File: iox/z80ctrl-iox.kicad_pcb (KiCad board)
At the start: 2 copper layers, 99.8 x 49.9 mm, 29 parts, among them J1 BUS, J10 GPIO_A, J11 RESET, J2 BUSEXT, J3 SPI1, J4 SPI2, J5 SPI3, J6 SPI4, J7 GPIO_B, J8 GPIO_C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

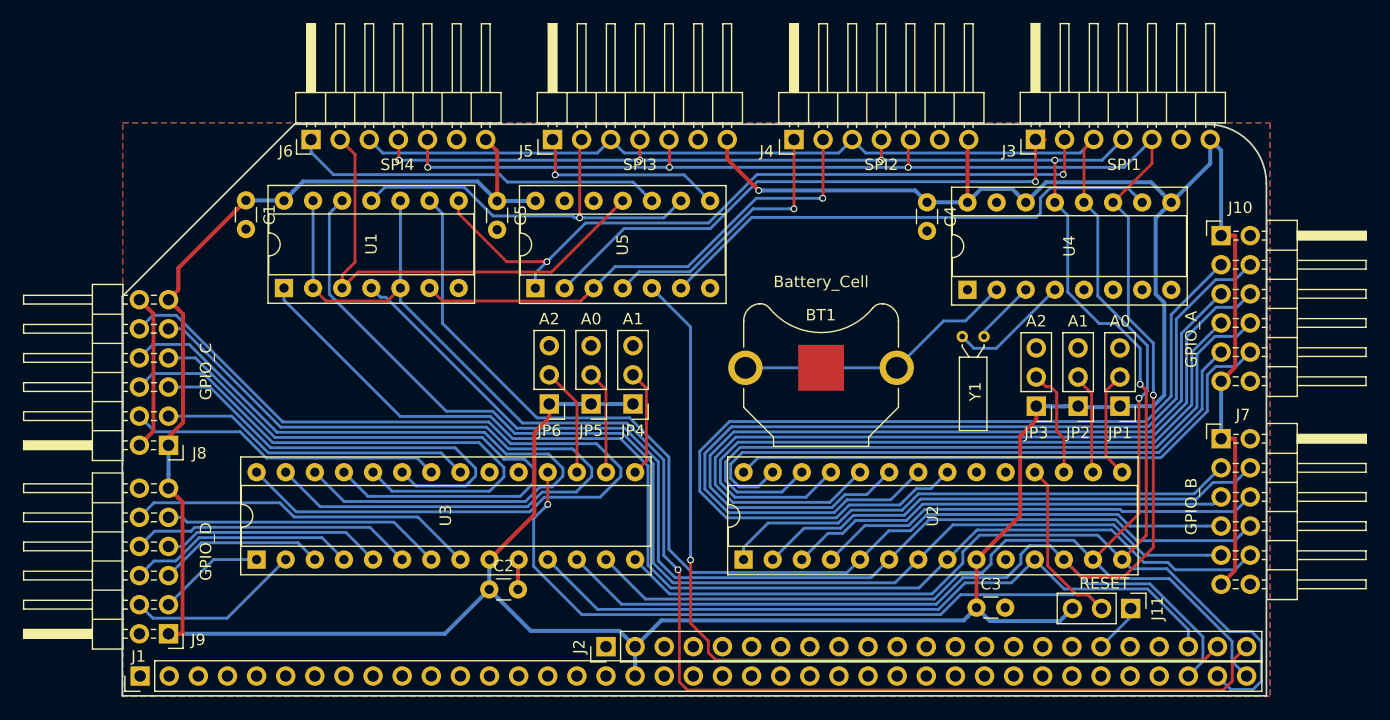
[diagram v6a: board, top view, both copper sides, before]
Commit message: Upgrade Kicad projects to v6
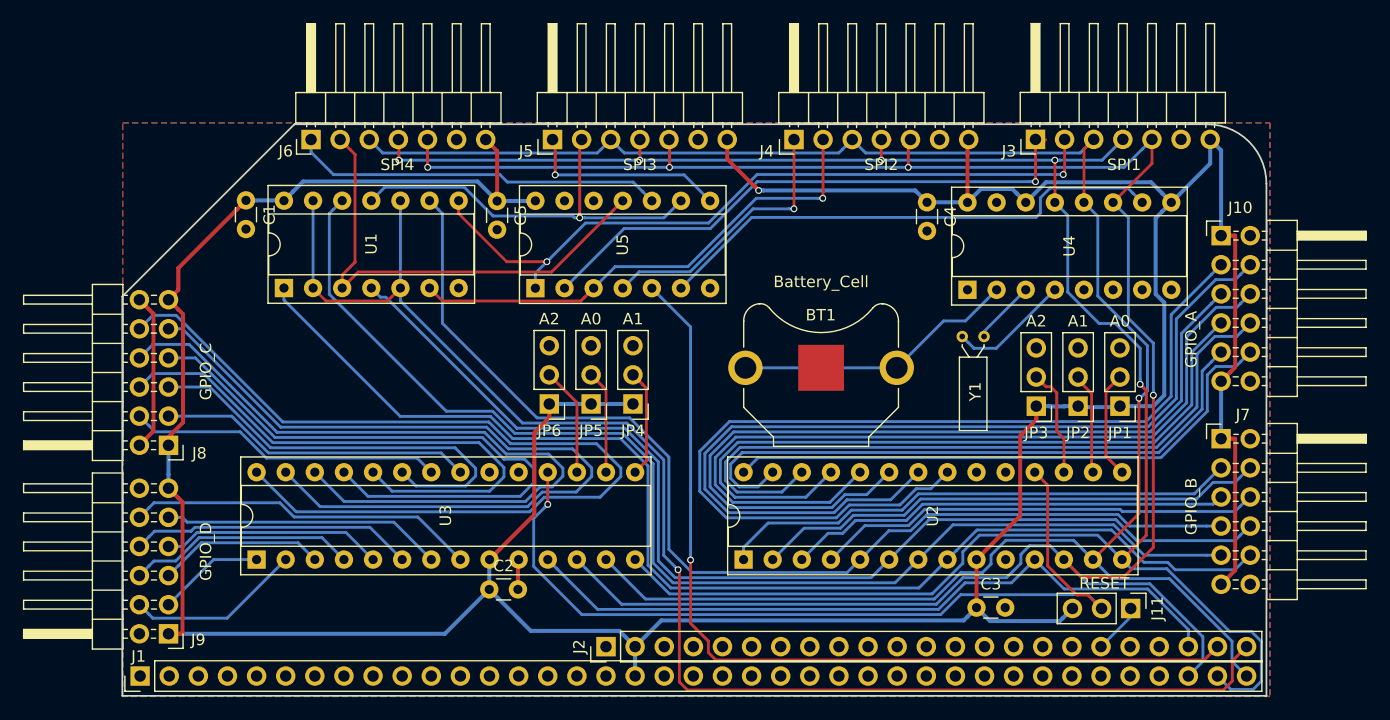
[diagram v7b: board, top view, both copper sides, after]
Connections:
- net /~AUXCS1~ renamed /~{AUXCS1}
- net /~AUXCS2~ renamed /~{AUXCS2}
- net /~AVRRST~ renamed /~{AVRRST}
- net /~EXTCS1~ renamed /~{EXTCS1}
- net /~EXTCS2~ renamed /~{EXTCS2}
- net /~EXTCS3~ renamed /~{EXTCS3}
- net /~EXTCS4~ renamed /~{EXTCS4}
- net /~IOXCS~ renamed /~{IOXCS}
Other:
- net class Default removed
- net class Power removed
